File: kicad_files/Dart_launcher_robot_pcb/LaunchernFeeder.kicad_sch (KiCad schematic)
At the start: 8 parts, among them J13 Conn_01x03_Pin, J14 Conn_01x03_Pin, J15 Conn_01x04_Pin, J17 Conn_01x03_Pin, J18 Conn_01x03_Pin, J19 Conn_01x03_Pin, J20 Conn_01x03_Pin, J21 Conn_01x03_Pin

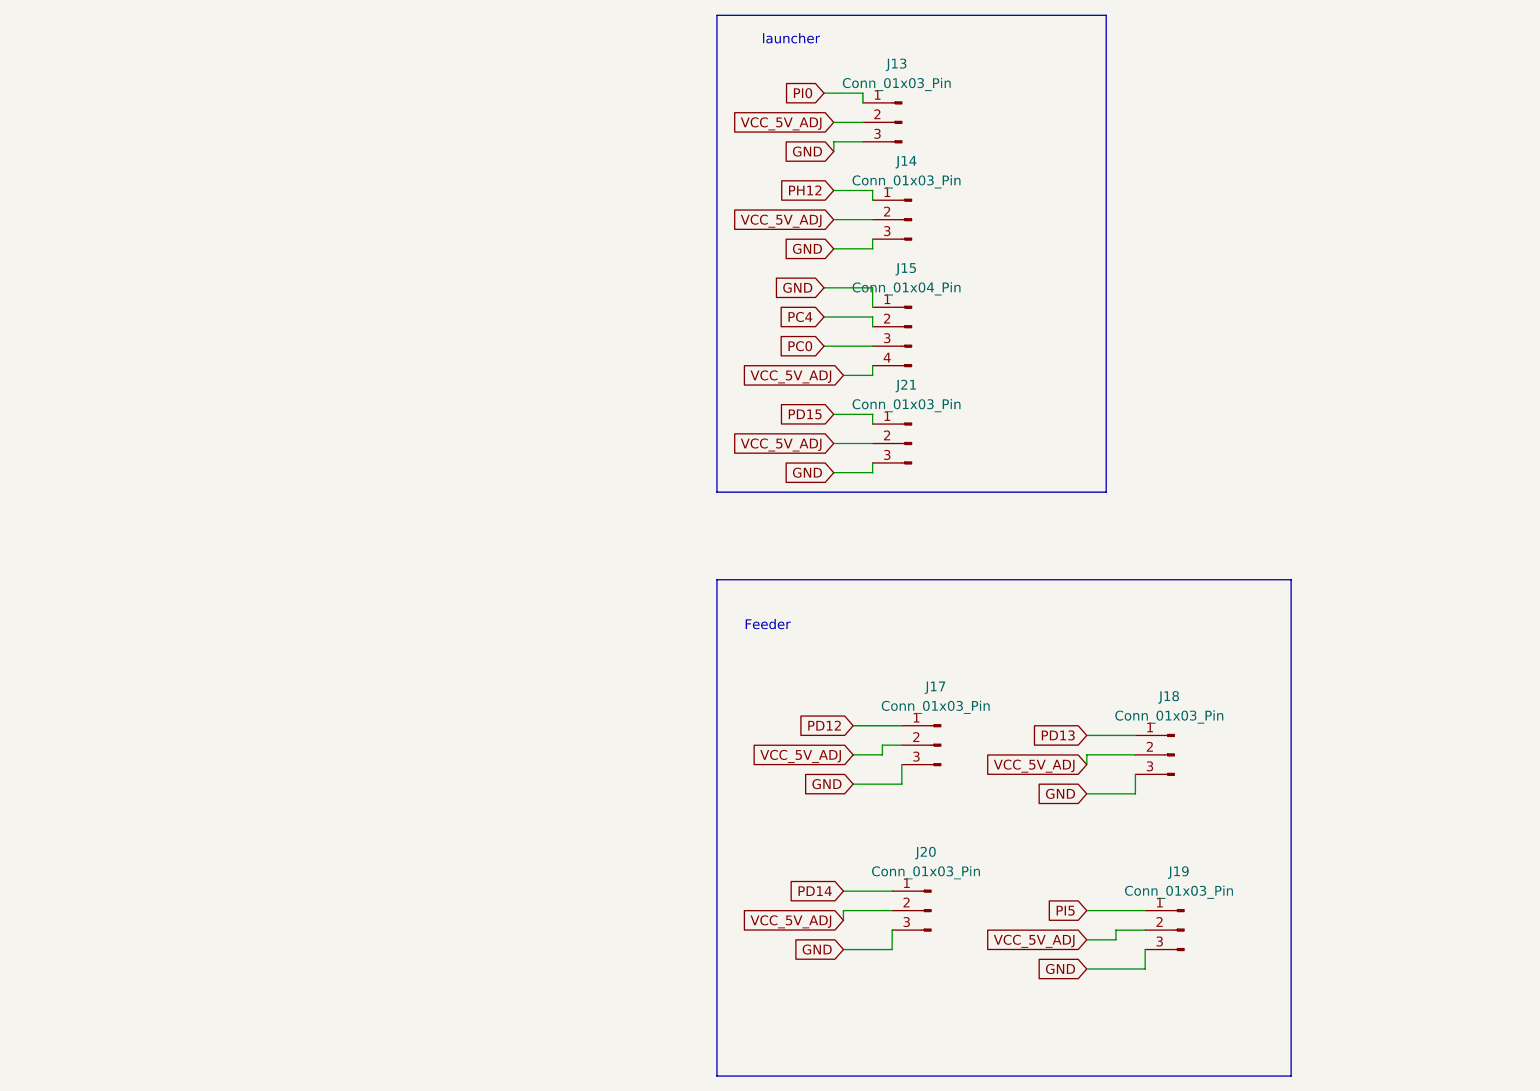
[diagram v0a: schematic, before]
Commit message: pcb design and changes to the pitch_yaw_launcher_code
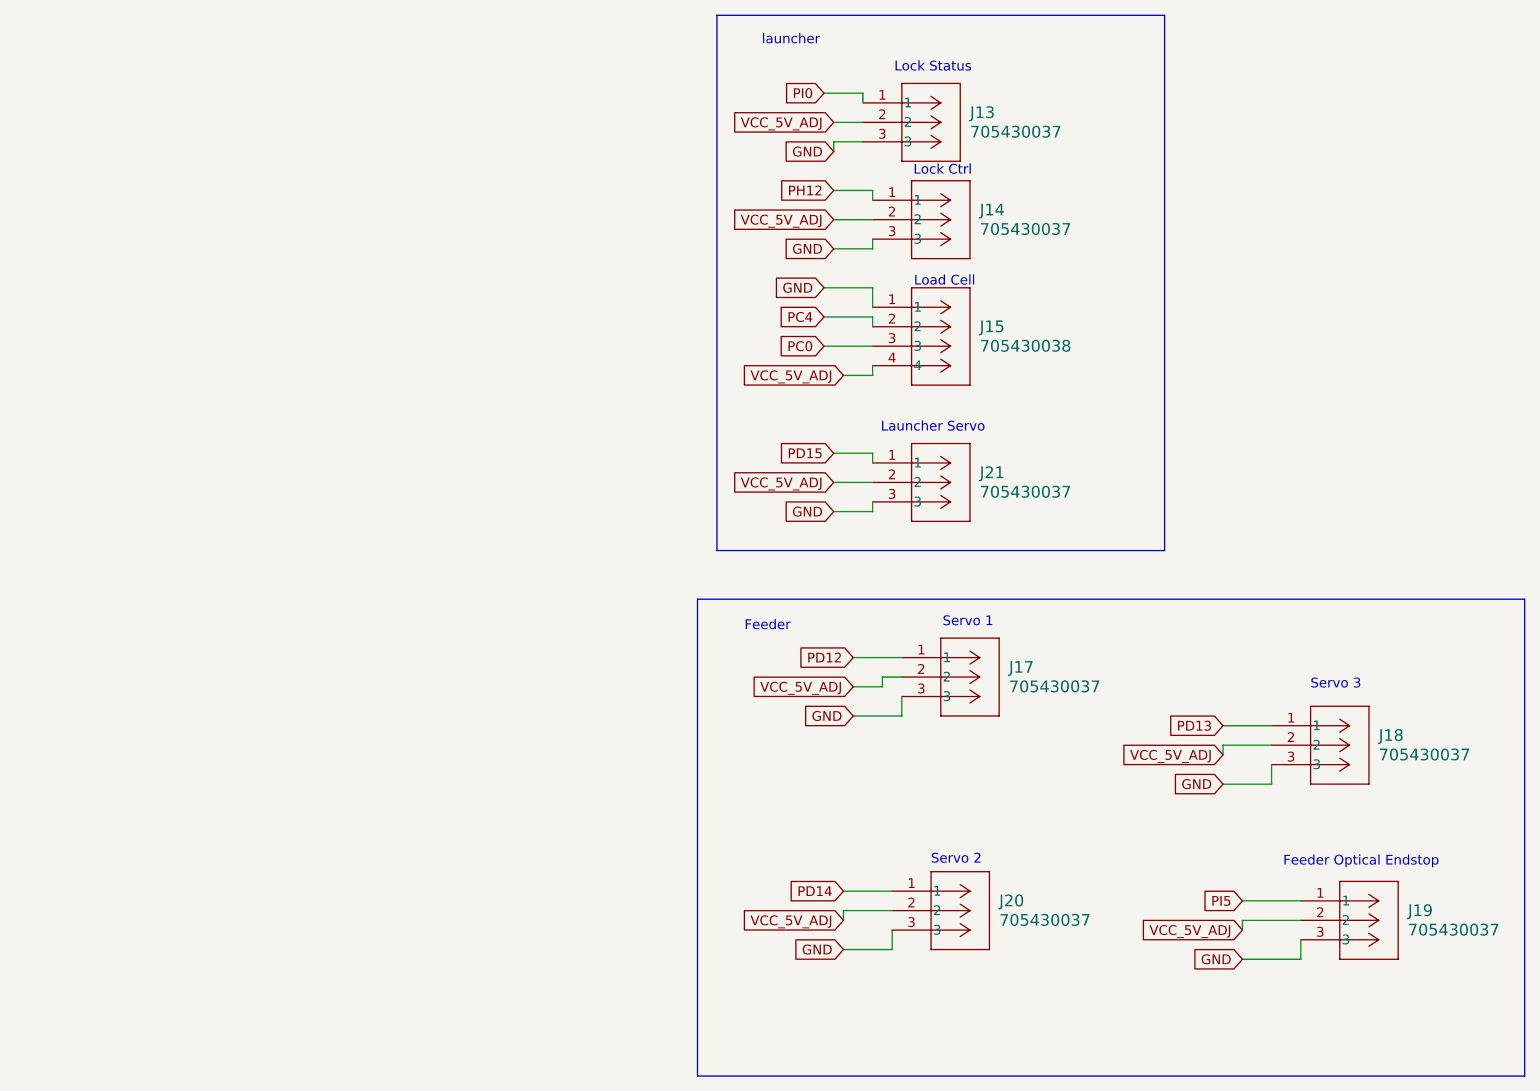
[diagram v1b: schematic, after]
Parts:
- removed J13, J14, J17, J18, J19, J20, J21: Conn_01x03_Pin, Connector_PinHeader_2.54mm:PinHeader_1x03_P2.54mm_Vertical, symbol Connector:Conn_01x03_Pin
- removed J15: Conn_01x04_Pin, Connector_PinHeader_2.54mm:PinHeader_1x04_P2.54mm_Vertical, symbol Connector:Conn_01x04_Pin
- added J13, J14, J17, J18, J19, J20, J21: 705430037, CONN_SDA-70543-xxxx_03_MOL, symbol Molex_0705430037:705430037
- added J15: 705430038, CONN_SDA-70543-xxxx_04_MOL, symbol Molex_705430038:705430038
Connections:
- net GND: now also J13.3, J14.3, J15.1, J17.3, J18.3, J19.3, J20.3, J21.3
- net PC0: now also J15.3
- net PC4: now also J15.2
- net PD12: now also J17.1
- net PD13: now also J18.1
- net PD14: now also J20.1
- net PD15: now also J21.1
- net PH12: now also J14.1
- net PI0: now also J13.1
- net PI5: now also J19.1
- net VCC_5V_ADJ: now also J13.2, J14.2, J15.4, J17.2, J18.2, J19.2, J20.2, J21.2
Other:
- note added: "Feeder Optical Endstop"
- note added: "Launcher Servo"
- note added: "Load Cell"
- note added: "Lock Ctrl"
- note added: "Lock Status"
- note added: "Servo 1"
- note added: "Servo 2"
- note added: "Servo 3"

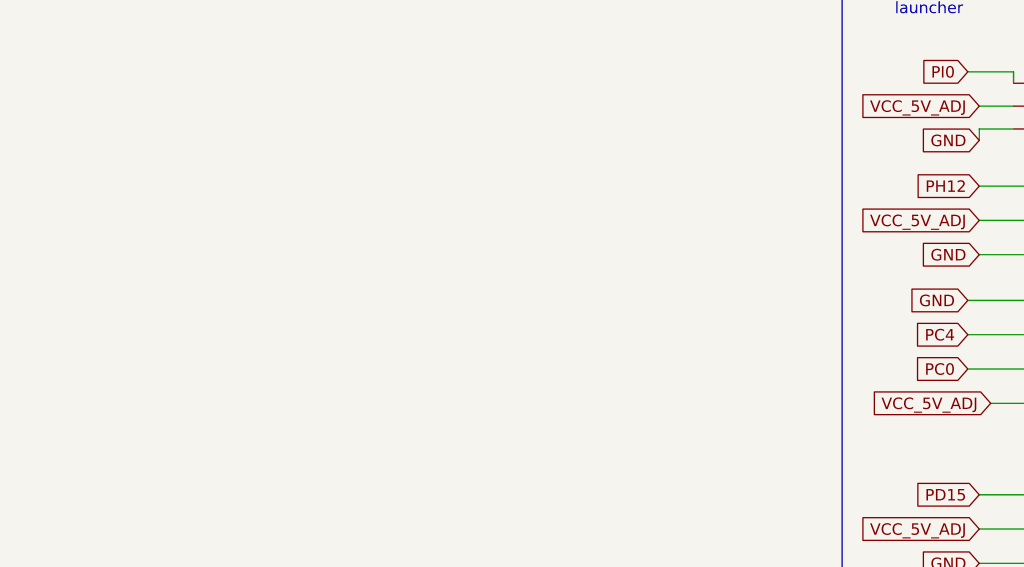
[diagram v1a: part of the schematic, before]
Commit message: the launcher task canabalise the  feeder task
update the frequency of the communication  to handle longer cable length

update the pitch yaw to handle  control of all the different type of control method

update screen to have an auto tab and a rc tab
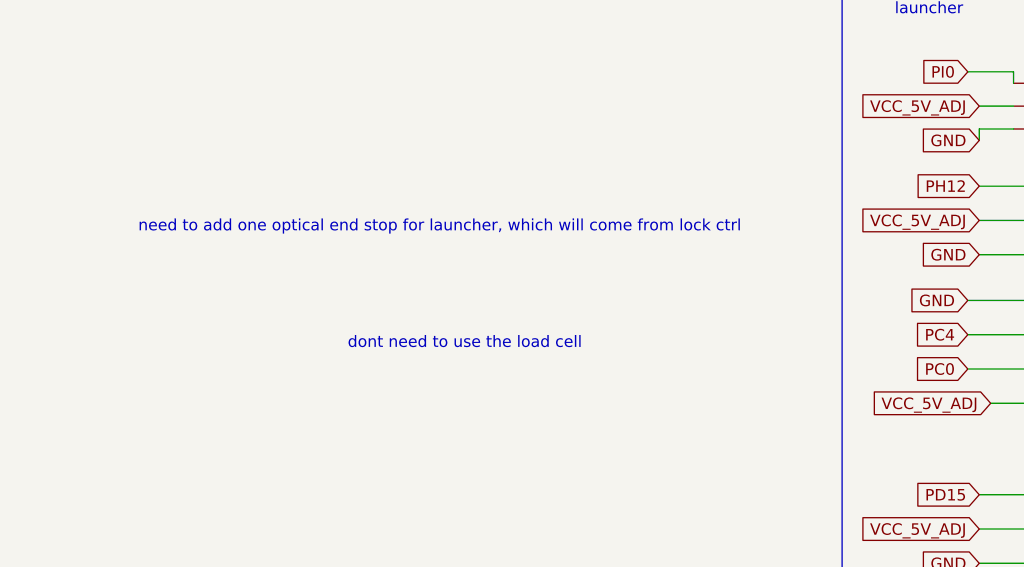
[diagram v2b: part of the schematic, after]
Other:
- note added: "dont need to use the load cell"
- note added: "need to add one optical end stop for launcher, which will come from lock ctrl"
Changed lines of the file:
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@@
+		)
+	)
+	(text "need to add one optical end stop for launcher, which will come from lock ctrl"
+		(exclude_from_sim no)
+		(at 55.626 51.562 0)
+		(effects
+			(font
+				(size 1.27 1.27)
+			)
 		)
 	)
@@
 		(effects
 			(font
+				(size 1.27 1.27)
+			)
+		)
+	)
+	(text "dont need to use the load cell"
+		(exclude_from_sim no)
+		(at 58.42 64.516 0)
+		(effects
+			(font
